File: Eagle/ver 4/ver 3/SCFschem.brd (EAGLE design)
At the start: 56.1 x 20.3 mm, 9 parts

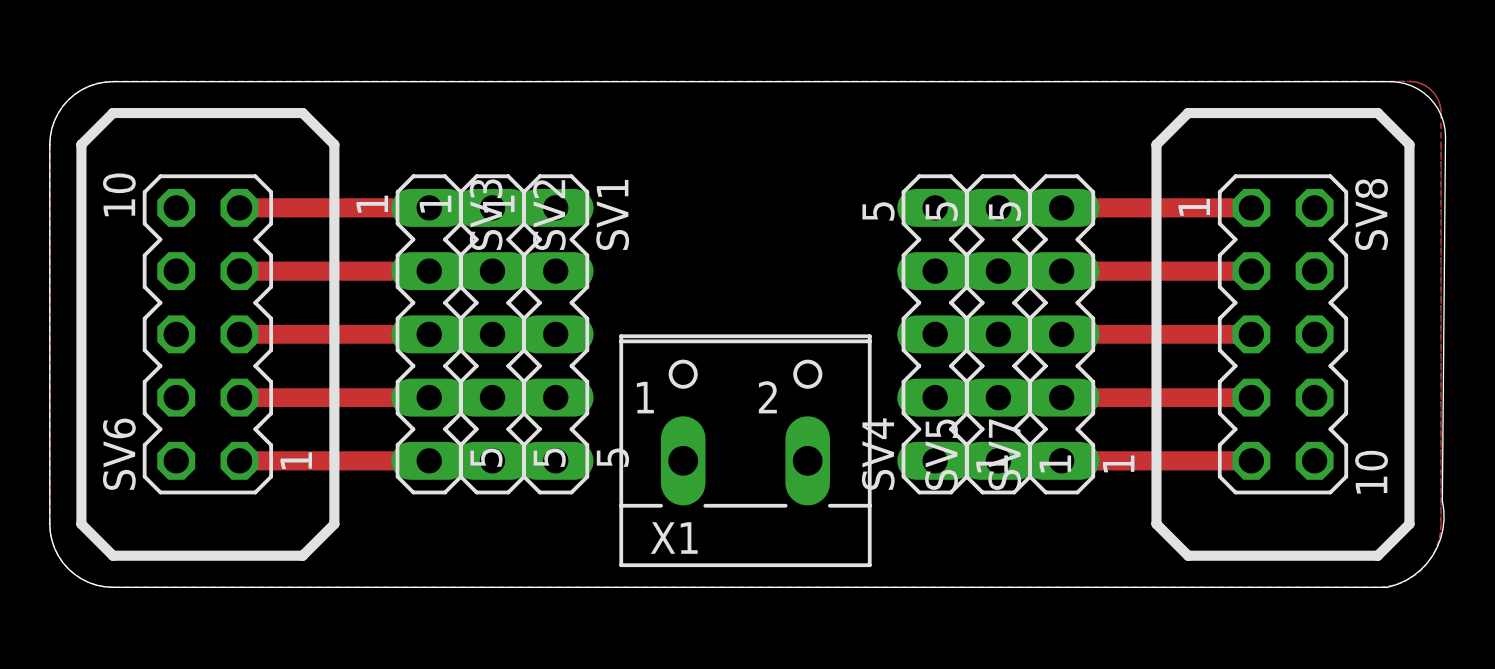
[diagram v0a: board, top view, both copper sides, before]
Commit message: Updated Ribbon Boards and revamped Shield
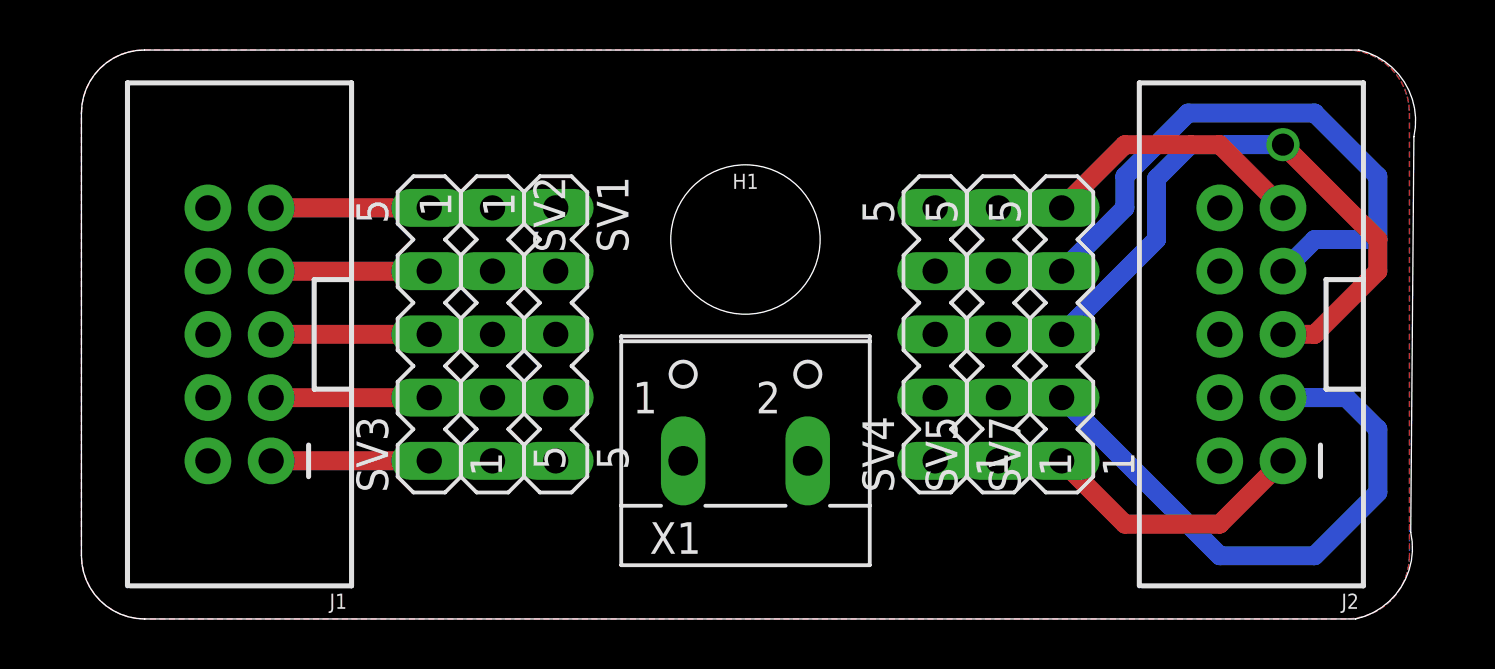
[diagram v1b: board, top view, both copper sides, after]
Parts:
- removed SV6, SV8: (no value), con-lstb:MA05-2
- added H1: STAND-OFF-NEWNEW, SparkFun-Hardware:STAND-OFF-NEW
- added J1, J2: AVR_SPI_PROG_5X2_NEWPTH2, SparkFun-Connectors:2X5-SHROUDED
- turned SV3 to 90 degrees
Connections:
- net GND: now also J1.10, J1.2, J1.4, J1.6, J1.8, J2.10, J2.2, J2.4, J2.6, J2.8; no longer SV6.10, SV6.2, SV6.4, SV6.6, SV6.8, SV8.10, SV8.2, SV8.4, SV8.6, SV8.8
- net S1: now also J1.1; no longer SV6.9
- net S10: now also J2.9; no longer SV8.1
- net S2: now also J1.3; no longer SV6.7
- net S3: now also J1.5; no longer SV6.5
- net S4: now also J1.7; no longer SV6.3
- net S5: now also J1.9; no longer SV6.1
- net S6: now also J2.1; no longer SV8.9
- net S7: now also J2.3; no longer SV8.7
- net S8: now also J2.5; no longer SV8.5
- net S9: now also J2.7; no longer SV8.3
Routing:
- net S8: track 7.62 -> 25.0 mm, vias 0 -> 1
- net S9: track 7.62 -> 24.0 mm
- net S7: track 7.62 -> 23.3 mm
- net S6: track 7.62 -> 11.0 mm
- net S10: track 7.62 -> 11.0 mm
- net S5: track 7.62 -> 6.35 mm
- net S4: track 7.62 -> 6.35 mm
- net S3: track 7.62 -> 6.35 mm
- net S2: track 7.62 -> 6.35 mm
- net S1: track 7.62 -> 6.35 mm
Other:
- board size 56.1 x 20.3 mm -> 53.6 x 22.8 mm
